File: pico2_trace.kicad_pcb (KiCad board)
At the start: 2 copper layers, 65 x 34 mm, 0 parts

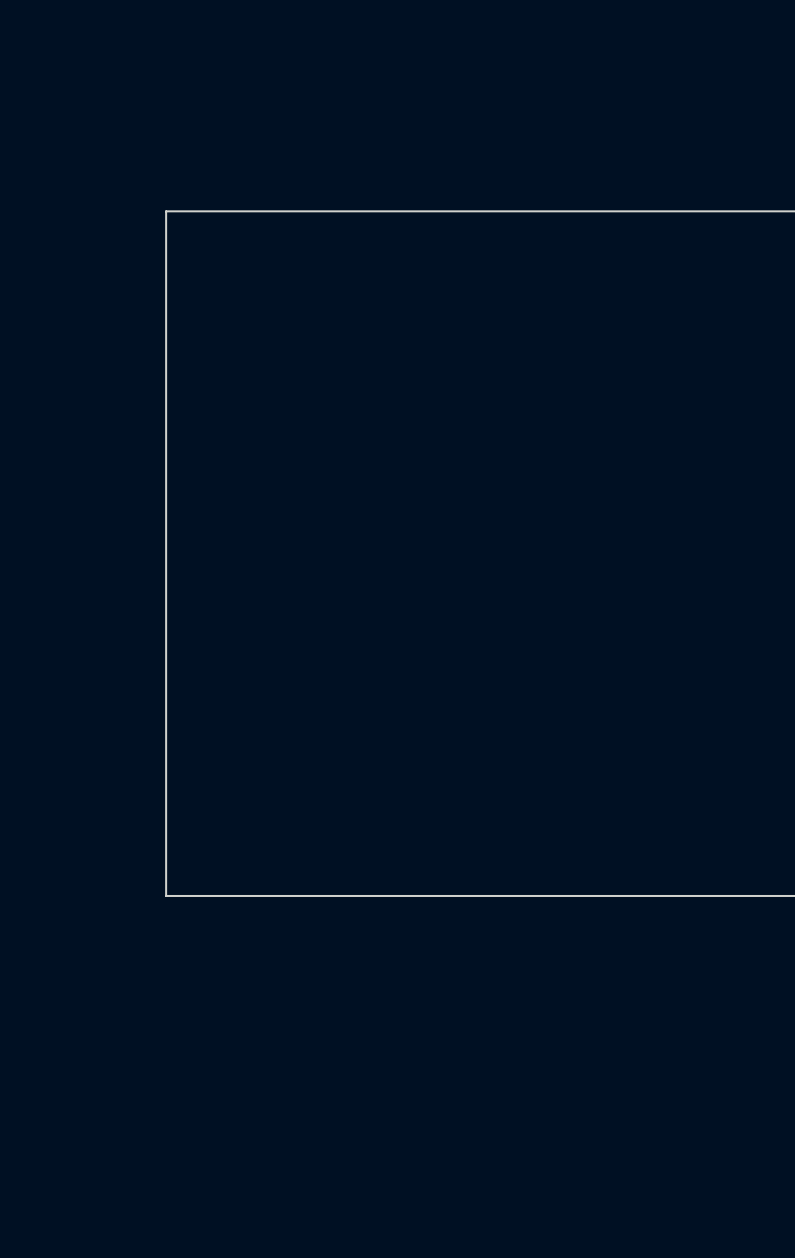
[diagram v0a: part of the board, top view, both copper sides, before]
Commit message: pcb: footprints, nets, net classes (persisted), 2-layer stackup
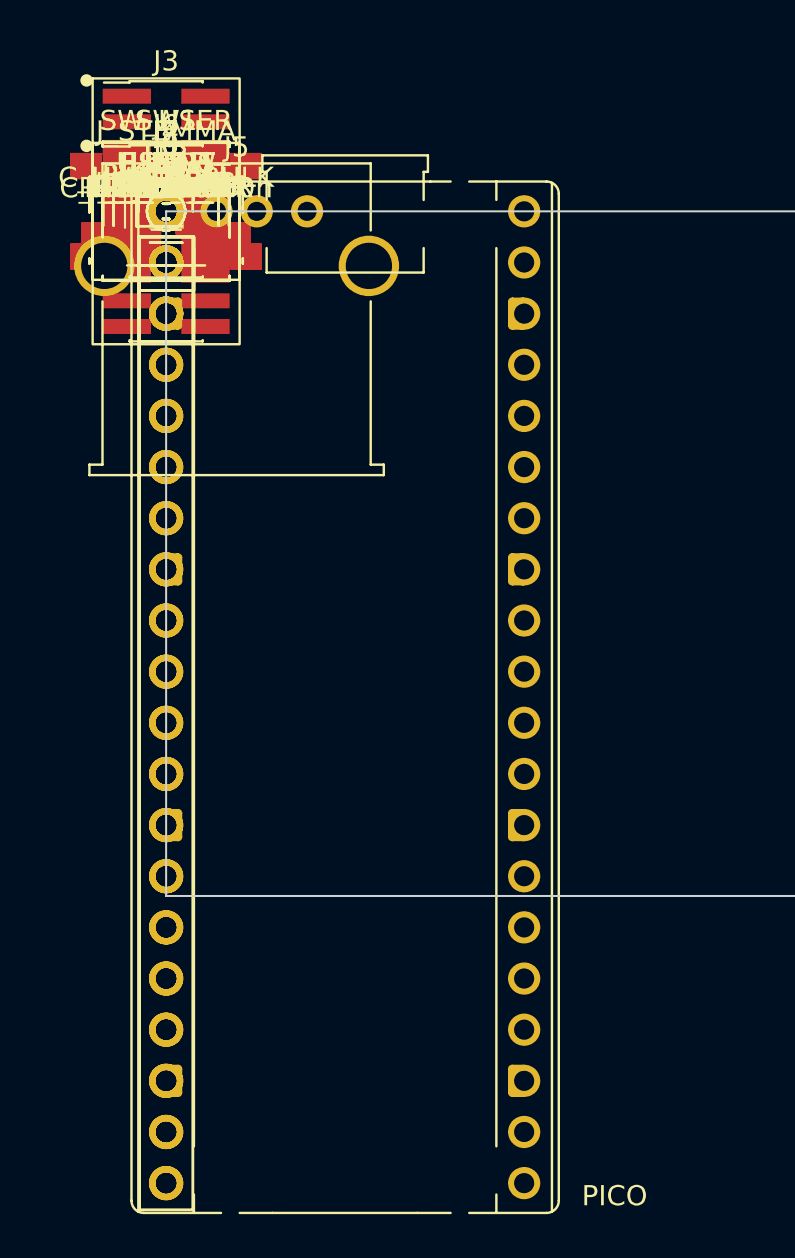
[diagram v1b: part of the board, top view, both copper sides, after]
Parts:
- added C_HVBUS_100n: 100n, C_0402_1005Metric, F.Cu at (0.00, 0.00)
- added C_HVBUS_BULK: 22u, C_0805_2012Metric, F.Cu at (0.00, 0.00)
- added ESD_D, ESD_H: USBLC6-2SC6, SOT-23-6, F.Cu at (0.00, 0.00)
- added J1B, J2B: BREAKOUT, PinSocket_1x20_P2.54mm_Vertical, F.Cu at (0.00, 0.00)
- added J3: MIPI-20, FTSH-110-01-DV, F.Cu at (0.00, 0.00)
- added J4: JST-SH-3 DEBUG, JST_SH_SM03B-SRSS-TB_1x03-1MP_P1.00mm_Horizontal, F.Cu at (0.00, 0.00)
- added J5: USB-A HOST, USB_A_Molex_67643_Horizontal, F.Cu at (0.00, 0.00)
- added J6: CORTEX-10, FTSH-105-01-DV, F.Cu at (0.00, 0.00)
- added J7: JST-SH-3 DEBUG_PROBE, JST_SH_SM03B-SRSS-TB_1x03-1MP_P1.00mm_Horizontal, F.Cu at (0.00, 0.00)
- added J8: USB-MICROB PWR, USB_Micro-B_Molex_47346-0001, F.Cu at (0.00, 0.00)
- added J9: USB-MICROB DEV, USB_Micro-B_Molex_47346-0001, F.Cu at (0.00, 0.00)
- added JP1: 5V SEL, PinHeader_1x03_P2.54mm_Vertical, F.Cu at (0.00, 0.00)
- added JP2: GP0 GUARD, PinHeader_1x02_P2.54mm_Vertical, F.Cu at (0.00, 0.00)
- added JP3: GP6 GUARD, PinHeader_1x02_P2.54mm_Vertical, F.Cu at (0.00, 0.00)
- added JP4: VBUS_DET EN, PinHeader_1x02_P2.54mm_Vertical, F.Cu at (0.00, 0.00)
- added J_STEMMA: STEMMA-QT, JST_SH_SM04B-SRSS-TB_1x04-1MP_P1.00mm_Horizontal, F.Cu at (0.00, 0.00)
- added J_UART: UART0, PinHeader_1x03_P2.54mm_Vertical, F.Cu at (0.00, 0.00)
- added LED_PWR, LED_USER: LED, LED_0603_1608Metric, F.Cu at (0.00, 0.00)
- added PICO: Pico2, RaspberryPi_Pico_Common_THT, F.Cu at (0.00, 0.00)
- added R_DDM, R_DDP, R_HDM, R_HDP: 22, R_0402_1005Metric, F.Cu at (0.00, 0.00)
- added R_DPU: 1.5k, R_0402_1005Metric, F.Cu at (0.00, 0.00)
- added R_HDM_PD, R_HDP_PD: 15k, R_0402_1005Metric, F.Cu at (0.00, 0.00)
- added R_J9VD_B, R_J9VD_T, R_NVD_B, R_NVD_T: 8.2k, R_0402_1005Metric, F.Cu at (0.00, 0.00)
- added R_LED_PWR, R_LED_USER: 1k, R_0402_1005Metric, F.Cu at (0.00, 0.00)
- added R_SHUNT: 0.1, R_1206_3216Metric, F.Cu at (0.00, 0.00)
- added Rt1, Rt2, Rt3, Rt4, Rt5: 27, R_0402_1005Metric, F.Cu at (0.00, 0.00)
- added SW1: RESET, SW_SPST_B3S-1000, F.Cu at (0.00, 0.00)
- added SW_USER: USER, SW_SPST_B3S-1000, F.Cu at (0.00, 0.00)
- added TP1, TP2, TP3: TP, TestPoint_Pad_D1.5mm, F.Cu at (0.00, 0.00)
- added U_HSW: TPS2051B, SOT-23-5, F.Cu at (0.00, 0.00)
- added U_ISNS: INA180A1DBVR, SOT-23-5, F.Cu at (0.00, 0.00)

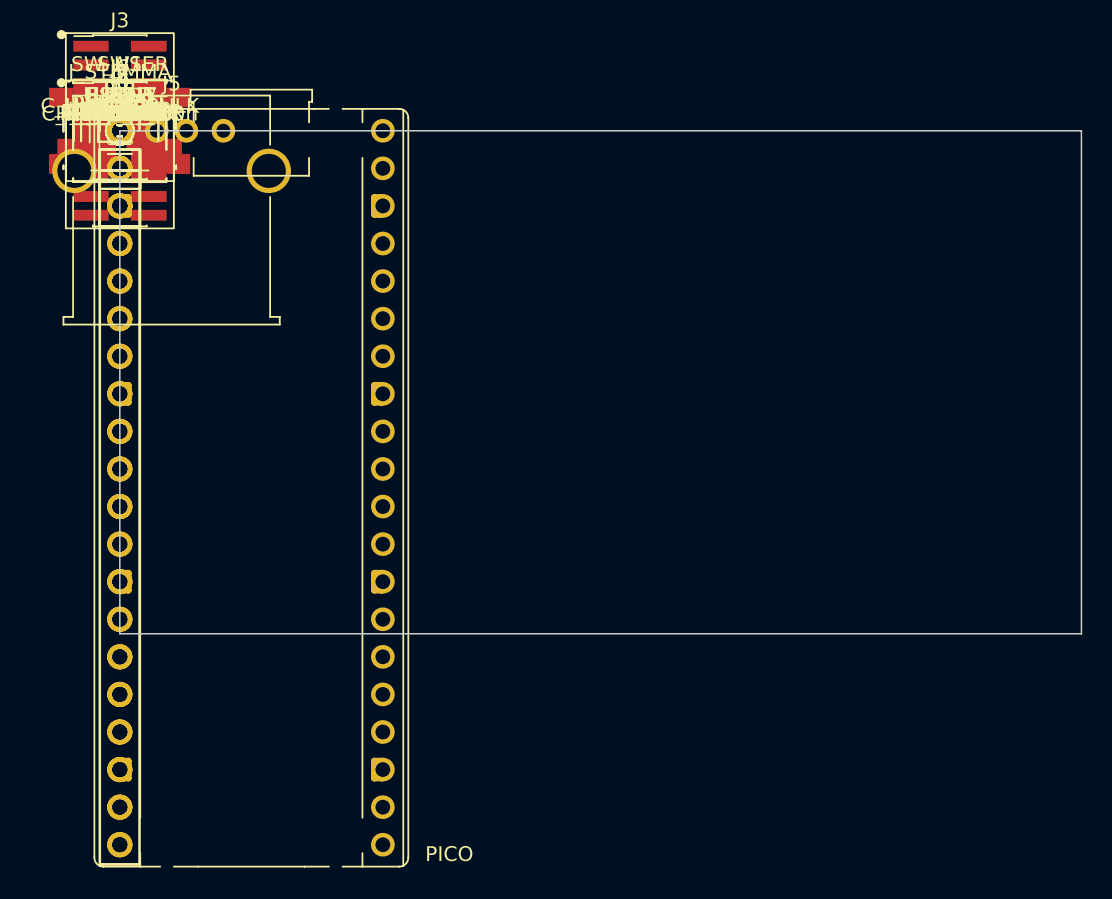
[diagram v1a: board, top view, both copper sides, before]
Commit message: pcb: outline, mounting holes, Pico socket edge
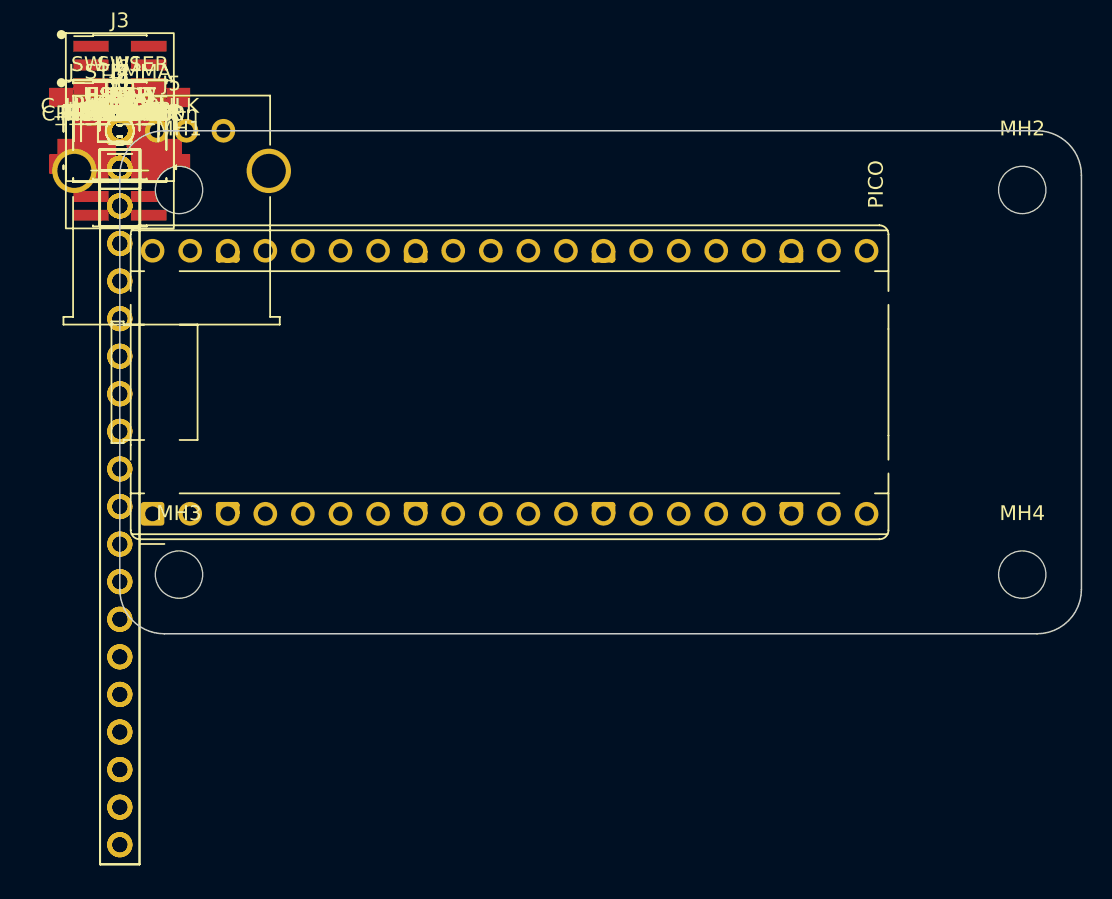
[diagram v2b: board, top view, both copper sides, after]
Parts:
- added MH1: MountingHole_3.2mm_M3, MountingHole_3.2mm_M3, F.Cu at (4.00, 4.00)
- added MH2: MountingHole_3.2mm_M3, MountingHole_3.2mm_M3, F.Cu at (61.0, 4.00)
- added MH3: MountingHole_3.2mm_M3, MountingHole_3.2mm_M3, F.Cu at (4.00, 30.0)
- added MH4: MountingHole_3.2mm_M3, MountingHole_3.2mm_M3, F.Cu at (61.0, 30.0)
- moved PICO 26.0 mm to (2.21, 25.9), turned to 90 degrees
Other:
- outline, holes or cut-outs redrawn

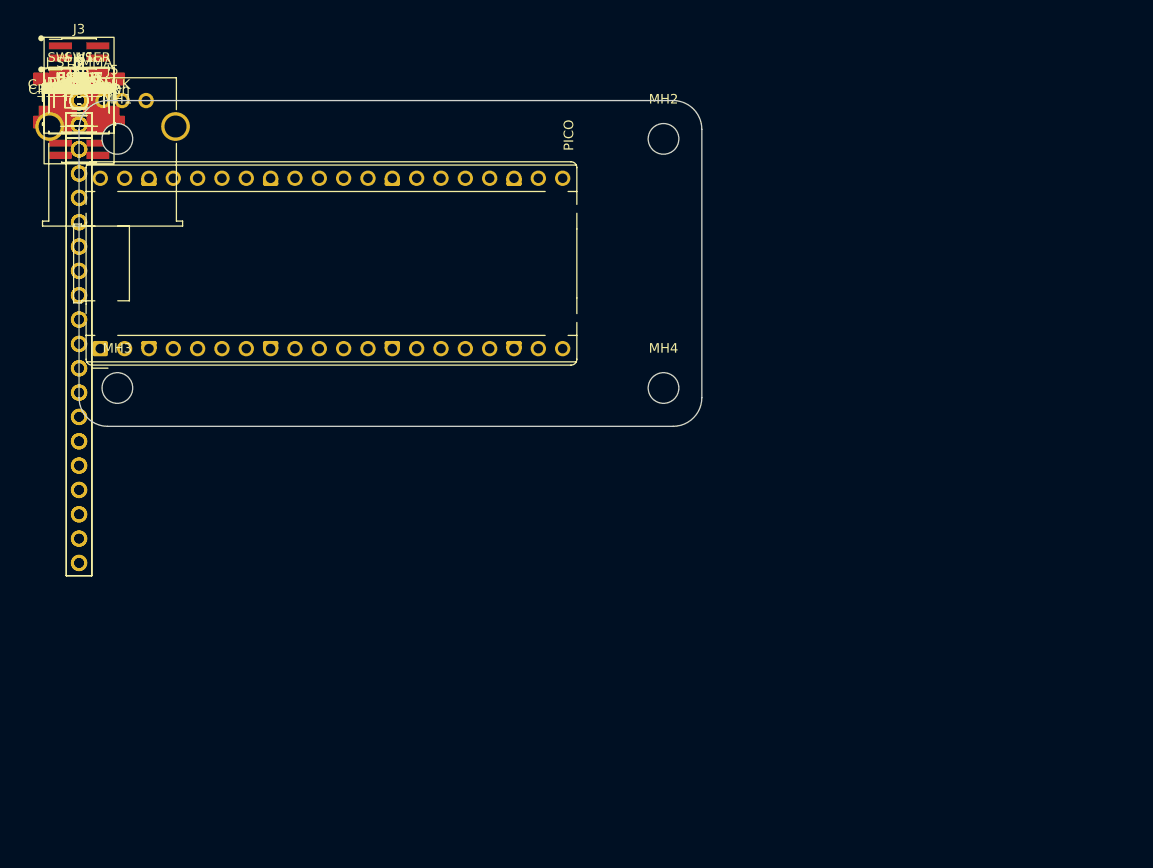
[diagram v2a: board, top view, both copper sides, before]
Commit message: pcb: constrained placement + trace silk
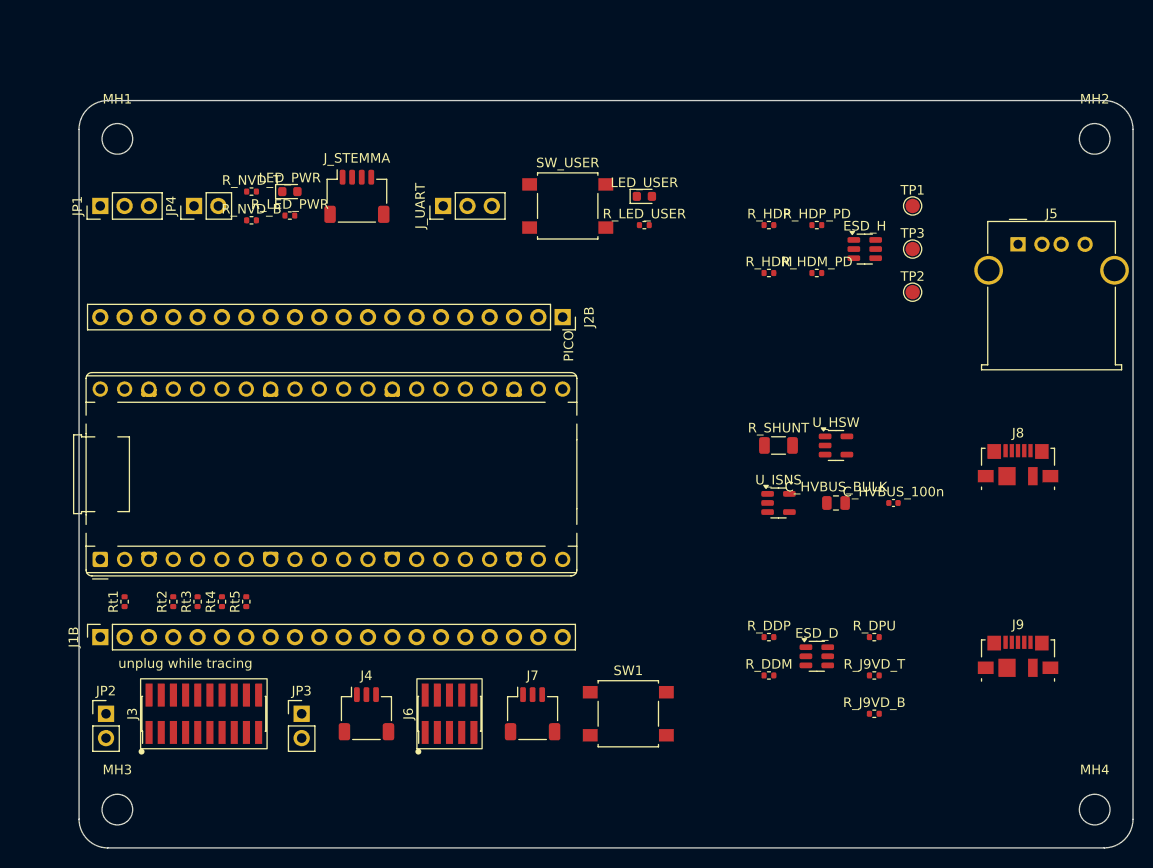
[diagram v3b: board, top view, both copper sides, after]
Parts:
- moved J9 113.9 mm to (98.0, 58.0)
- moved J8 105.1 mm to (98.0, 38.0)
- moved R_J9VD_B 104.8 mm to (83.0, 64.0)
- moved R_J9VD_T 102.4 mm to (83.0, 60.0)
- moved R_DPU 100.1 mm to (83.0, 56.0)
- moved J5 99.1 mm to (98.0, 15.0)
- moved ESD_D 96.4 mm to (77.0, 58.0)
- moved C_HVBUS_100n 94.8 mm to (85.0, 42.0)
- moved R_DDM 93.7 mm to (72.0, 60.0)
- moved R_DDP 91.2 mm to (72.0, 56.0)
- moved C_HVBUS_BULK 89.5 mm to (79.0, 42.0)
- moved TP2 89.3 mm to (87.0, 20.0)
- moved TP3 88.4 mm to (87.0, 15.5)
- moved TP1 87.7 mm to (87.0, 11.0)
- moved U_HSW 86.8 mm to (79.0, 36.0)
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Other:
- board size 65 x 34 mm -> 110 x 78 mm
- board text added: "unplug while tracing"

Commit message: pcb: rotate edge connectors to face board edges (review fix)
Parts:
- moved ESD_D 9.17 mm to (85.3, 62.0)
- moved J8 9.17 mm to (106.3, 42.0), turned to 90 degrees
- moved J9 9.17 mm to (106.3, 62.0), turned to 90 degrees
- moved R_DDM 9.17 mm to (80.3, 64.0)
- moved R_DDP 9.17 mm to (80.3, 60.0)
- moved R_DPU 9.17 mm to (91.3, 60.0)
- moved R_J9VD_B 9.17 mm to (91.3, 68.0)
- moved R_J9VD_T 9.17 mm to (91.3, 64.0)
- moved ESD_H 6.65 mm to (80.6, 22.0)
- moved J5 6.65 mm to (96.6, 21.5), turned to 90 degrees
- moved R_HDM 6.65 mm to (70.6, 24.5)
- moved R_HDM_PD 6.65 mm to (75.6, 24.5)
- moved R_HDP 6.65 mm to (70.6, 19.5)
- moved R_HDP_PD 6.65 mm to (75.6, 19.5)
- moved TP1 6.65 mm to (85.6, 17.5)
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
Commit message: pcb: length-matched trace bundle + SWD
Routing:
- net NRESET: track 0.00 -> 109.3 mm, vias 0 -> 9
- net P3V3: track 0.00 -> 87.9 mm, vias 0 -> 6
- net SWDIO: track 0.00 -> 71.7 mm, vias 0 -> 4
- net SWCLK: track 0.00 -> 69.2 mm, vias 0 -> 12
- net TD1: track 0.00 -> 19.6 mm
- net TD2: track 0.00 -> 19.2 mm
- net TRACECLK: track 0.00 -> 19.0 mm
- net TD3: track 0.00 -> 18.9 mm
- net TD0: track 0.00 -> 18.7 mm
- net GP4: track 0.00 -> 6.36 mm
- net GP3: track 0.00 -> 6.36 mm
- net GP1: track 0.00 -> 6.36 mm
- net GP2: track 0.00 -> 6.36 mm
- net GP5: track 0.00 -> 6.36 mm

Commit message: pcb: route power, USB pairs, guards; finish bulk nets
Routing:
- net VBUS_NET: track 0.00 -> 171.2 mm, vias 0 -> 2
- net VBUS_SEL: track 0.00 -> 108.3 mm, vias 0 -> 2
- net NATIVE_VBUS_DET: track 0.00 -> 61.3 mm
- net HOST_VBUS: track 0.00 -> 48.0 mm, vias 0 -> 2
- net P3V3: track 87.9 -> 129.8 mm, vias 6 -> 8
- net HOST_DM: track 0.00 -> 30.7 mm
- net DEV_DP: track 0.00 -> 28.8 mm
- net HOST_DP: track 0.00 -> 28.4 mm
- net J9_VBUS: track 0.00 -> 21.1 mm
- net HOST_5V_IN: track 0.00 -> 20.4 mm
- net GP6: track 0.00 -> 16.1 mm
- net GP0: track 0.00 -> 16.1 mm
- net BTN_USER: track 0.00 -> 16.1 mm
- net NRESET: track 109.3 -> 124.8 mm
- net DEV_VBUS_DET: track 0.00 -> 11.6 mm
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
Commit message: model: realize DNP parts (INA219 opt), EN pulldown, cap ratings, J9_VBUS class
- Add R_HVEN_PD (100k, HOST_VBUS_EN->GND): RP2350-E9 makes the chip's own
  internal pull-downs unreliable before firmware runs, so the TPS2051B EN
  pin needs a real external pulldown to default the host load switch off
  at boot.
- Capacitor values now carry voltage ratings (Adafruit schematic rule):
  C_HVBUS_BULK 22u -> 22u/10V, C_HVBUS_100n/C_NRESET 100n -> 100n/16V.
- Realize the DNP parts Adafruit-style (real footprint + fully wired +
  dnp=True, instead of a stand-in footprint with all pins no-connect):
  U_INA219_ALT gets the real INA219 SOT-23-8 footprint/padmap (TI SBOS448
  Fig 8-1) and is wired across the same shunt as U_ISNS, on the shared
  I2C0 bus, address 0x40. D_J9_BUSPWR/J_TRACE_TP were already wired.
  emit_netlist, gen_sch.py, and build_board.py now include/place/wire DNP
  parts instead of omitting them (KiCad 9 dnp=yes symbol attribute;
  FP_DNP + FP_EXCLUDE_FROM_POS_FILES footprint attribute, still shown in
  BOM). They land at (0,0) for now -- a follow-up compaction/placement
  pass places them for real.
- Add J9_VBUS to the Power netclass pattern list (missing since Task 14).
- docs/PARTS.md: the three Adafruit-component-reuse evaluations (TPS2051B
  kept over AP22802, USBLC6-2SC6 kept over PRTR5V0U2X, INA219 adopted as
  a populatable DNP option), an LCSC-first sourcing note, and a Samtec
  FTSH <-> LCSC keyed-shroud alternate note for the debug headers.

Verified: 7/7 model tests, ERC 0 errors (67 pre-existing off-grid
warnings, unchanged), schematic/reference netlist parity match (DNP nodes
included on both sides), board rebuild idempotent. No geometry changed:
0 of 52 existing footprints moved and the Task 13/14 trace bundle is
byte-identical -- confirmed programmatically, not just by inspection.
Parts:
- added C_NRESET: 100n/16V, C_0402_1005Metric, F.Cu at (0.00, 0.00)
- added D_J9_BUSPWR: 1N4148W, D_SOD-123, F.Cu at (0.00, 0.00)
- added J_TRACE_TP: TRACE_TP, PinHeader_1x06_P2.54mm_Vertical, F.Cu at (0.00, 0.00)
- added R_HVEN_PD: 100k, R_0402_1005Metric, F.Cu at (0.00, 0.00)
- added U_INA219_ALT: INA219, SOT-23-8, F.Cu at (0.00, 0.00)
- C_HVBUS_100n: value 100n -> 100n/16V
- C_HVBUS_BULK: value 22u -> 22u/10V
